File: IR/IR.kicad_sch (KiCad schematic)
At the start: 211 parts

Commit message: 回路設計
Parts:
- removed U? (x15): TSSP58038, OptoDevice:Vishay_MINICAST-3Pin, symbol Sensor_Proximity:TSSP58038
- added U10, U11, U12, U13, U14, U15, U16, U17, U2, U3, U4, U6, U7, U8, U9: TSSP58038, TSSP58038:TSSP58038_LongPad, symbol Sensor_Proximity:TSSP58038
- D12, D13, D14, D15, D16, D17, D18, D19, D20, D21, D22, D23, D24, D25, D26, D27: renamed from D?; footprint (none) -> LED_THT:LED_D3.0mm_Horizontal_O1.27mm_Z2.0mm
- U1: renamed from U?; footprint OptoDevice:Vishay_MINICAST-3Pin -> TSSP58038:TSSP58038_LongPad
- gave numbers to parts that had none: 179
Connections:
- net +3.3V: now also U10.3 (Vs), U11.3 (Vs), U12.3 (Vs), U13.3 (Vs), U14.3 (Vs), U15.3 (Vs), U16.3 (Vs), U17.3 (Vs), U2.3 (Vs), U3.3 (Vs), U4.3 (Vs), U6.3 (Vs), U7.3 (Vs), U8.3 (Vs), U9.3 (Vs)
- net GND: now also U10.2 (GND), U11.2 (GND), U12.2 (GND), U13.2 (GND), U14.2 (GND), U15.2 (GND), U16.2 (GND), U17.2 (GND), U2.2 (GND), U3.2 (GND), U4.2 (GND), U6.2 (GND), U7.2 (GND), U8.2 (GND), U9.2 (GND)
- net IR_rcpt1: now also U2.1 (OUT)
- net IR_rcpt10: now also U12.1 (OUT)
- net IR_rcpt11: now also U13.1 (OUT)
- net IR_rcpt12: now also U14.1 (OUT)
- net IR_rcpt13: now also U15.1 (OUT)
- net IR_rcpt14: now also U16.1 (OUT)
- net IR_rcpt15: now also U17.1 (OUT)
- net IR_rcpt2: now also U3.1 (OUT)
- net IR_rcpt3: now also U4.1 (OUT)
- net IR_rcpt4: now also U6.1 (OUT)
- net IR_rcpt5: now also U7.1 (OUT)
- net IR_rcpt6: now also U8.1 (OUT)
- net IR_rcpt7: now also U9.1 (OUT)
- net IR_rcpt8: now also U10.1 (OUT)
- net IR_rcpt9: now also U11.1 (OUT)

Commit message: 構成図追加
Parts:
- removed J2: Conn_01x10_Female, Connector_IDC:IDC-Header_2x05_P2.54mm_Horizontal, symbol Connector:Conn_01x10_Female
- added J2: Conn_01x10_Male, BoxHeader_1.27mm:BoxHeader_2x05_P1.27mm_Vertical_SMD, symbol Connector:Conn_01x10_Male
- added R103, R104, R105: 5.1k, Resistor_SMD:R_0402_1005Metric, symbol Device:R
- added R106, R107, R108, R109: 10k, Resistor_SMD:R_0402_1005Metric, symbol Device:R
- Q11, Q12, Q5, Q7, Q9: value 2PB709AR -> S8050; footprint Package_TO_SOT_SMD:SC-59_Handsoldering -> Package_TO_SOT_SMD:SOT-23
- SW3: footprint (none) -> Slide_Switch:SW_Slide_SPDT_White
- Y1: footprint (none) -> Crystal:Crystal_SMD_HC49-SD_HandSoldering
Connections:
- net 3.3VBUS: now also J2.1 (Pin_1)
- net Blightness_2nd: now also R107.1
- net Blightness_3rd: now also R108.1
- net Blightness_Max: now also R106.1
- net Blightness_Min: now also R109.1
- net GND: now also R32.1, R33.1, J2.4 (Pin_4), R103.1, R104.1, R105.1, R106.2, R107.2, R108.2, R109.2; no longer R32.2, R33.2
- net MainRX_STLinkTX: now also J2.8 (Pin_8)
- net MainTX_STLinkRX: now also J2.9 (Pin_9)
- net Mux_IN0: now also R103.2
- net Mux_IN1: now also R104.2
- net Mux_IN2: now also R105.2
- net Mux_OUT0: now also R32.2; no longer R32.1
- net Mux_OUT1: now also R33.2; no longer R33.1
- net NRST: now also J2.6 (Pin_6)
- net TCK: now also J2.3 (Pin_3)
- net TMS: now also J2.5 (Pin_5)
- no-connect marks 19 -> 5
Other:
- note added: "PullDown"
- moved on the sheet: Q13, Q14, Q15, U18, U19

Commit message: diagram_SmallPW
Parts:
- removed C1, C14: 4.7uF, Capacitor_SMD:C_0603_1608Metric, symbol Device:C
- added C? (x2): 1uF, Capacitor_SMD:C_0402_1005Metric, symbol Device:C
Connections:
- net 3.3VSYS: now also C?.1
- net S-S: now also C?.1
- net at Q3.1 (G), R4.2, R8.1: now also C?.2
- net at Q8.1 (G), R22.2, R24.1: now also C?.2
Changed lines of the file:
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@@
     (pin "3")
   )
+  (symbol (lib_id "Device:C") (at 124.46 142.24 0) (unit 1)
+    (in_bom yes) (on_board yes) (fields_autoplaced)
+    (property "Reference" "C?" (id 0) (at 128.27 140.9699 0)
+      (effects (font (size 1.27 1.27)) (justify left))
+    )
+    (property "Value" "1uF" (id 1) (at 128.27 143.5099 0)
+      (effects (font (size 1.27 1.27)) (justify left))
+    )
+    (property "Footprint" "Capacitor_SMD:C_0402_1005Metric" (id 2) (at 125.4252 146.05 0)
+      (effects (font (size 1.27 1.27)) hide)
+    )
+    (property "Datasheet" "~" (id 3) (at 124.46 142.24 0)
+      (effects (font (size 1.27 1.27)) hide)
+    )
+    (pin "1")
+    (pin "2")
+  )
   (symbol (lib_id "power:GND") (at 355.6 109.22 0) (mirror y) (unit 1)
     (in_bom yes) (on_board yes)
@@
     (pin "2")
   )
-  (symbol (lib_id "Device:C") (at 248.92 86.36 0) (unit 1)
-    (in_bom yes) (on_board yes) (fields_autoplaced)
-    (property "Reference" "C14" (id 0) (at 252.73 85.0899 0)
-      (effects (font (size 1.27 1.27)) (justify left))
-    )
-    (property "Value" "4.7uF" (id 1) (at 252.73 87.6299 0)
-      (effects (font (size 1.27 1.27)) (justify left))
-    )
-    (property "Footprint" "Capacitor_SMD:C_0603_1608Metric" (id 2) (at 249.8852 90.17 0)
-      (effects (font (size 1.27 1.27)) hide)
-    )
-    (property "Datasheet" "~" (id 3) (at 248.92 86.36 0)
-      (effects (font (size 1.27 1.27)) hide)
-    )
-    (pin "1")
-    (pin "2")
-  )
   (symbol (lib_id "power:VDD") (at 721.36 248.92 0) (unit 1)
     (in_bom yes) (on_board yes) (fields_autoplaced)
@@
     (pin "2")
   )
+  (symbol (lib_id "Device:C") (at 248.92 86.36 0) (unit 1)
+    (in_bom yes) (on_board yes) (fields_autoplaced)
+    (property "Reference" "C?" (id 0) (at 252.73 85.0899 0)
+      (effects (font (size 1.27 1.27)) (justify left))
+    )
+    (property "Value" "1uF" (id 1) (at 252.73 87.6299 0)
+      (effects (font (size 1.27 1.27)) (justify left))
+    )
+    (property "Footprint" "Capacitor_SMD:C_0402_1005Metric" (id 2) (at 249.8852 90.17 0)
+      (effects (font (size 1.27 1.27)) hide)
+    )
+    (property "Datasheet" "~" (id 3) (at 248.92 86.36 0)
+      (effects (font (size 1.27 1.27)) hide)
+    )
+    (pin "1")
+    (pin "2")
+  )
   (symbol (lib_id "Device:R") (at 193.04 365.76 270) (mirror x) (unit 1)
     (in_bom yes) (on_board yes)
@@
     (pin "2")
   )
-  (symbol (lib_id "Device:C") (at 124.46 142.24 0) (unit 1)
-    (in_bom yes) (on_board yes) (fields_autoplaced)
-    (property "Reference" "C1" (id 0) (at 128.27 140.9699 0)
-      (effects (font (size 1.27 1.27)) (justify left))
-    )
-    (property "Value" "4.7uF" (id 1) (at 128.27 143.5099 0)
-      (effects (font (size 1.27 1.27)) (justify left))
-    )
-    (property "Footprint" "Capacitor_SMD:C_0603_1608Metric" (id 2) (at 125.4252 146.05 0)
-      (effects (font (size 1.27 1.27)) hide)
-    )
-    (property "Datasheet" "~" (id 3) (at 124.46 142.24 0)
-      (effects (font (size 1.27 1.27)) hide)
-    )
-    (pin "1")
-    (pin "2")
-  )
   (symbol (lib_id "Device:R") (at 607.06 386.08 0) (unit 1)
     (in_bom yes) (on_board yes)
@@
       (reference "#PWR0218") (unit 1) (value "+3.3V") (footprint "")
     )
-    (path "/d3fd32d8-94e9-4c99-93a7-2be4594e1c1d"
-      (reference "C1") (unit 1) (value "4.7uF") (footprint "Capacitor_SMD:C_0603_1608Metric")
-    )
     (path "/3be126c6-ab05-4a33-b739-124117490790"
       (reference "C2") (unit 1) (value "0.1uF") (footprint "Capacitor_SMD:C_0402_1005Metric")
@@
       (reference "C13") (unit 1) (value "ADJ_ST") (footprint "Capacitor_SMD:C_0603_1608Metric")
     )
-    (path "/7ac18cd6-3e4d-45f8-a364-a40e9c7e4e34"
-      (reference "C14") (unit 1) (value "4.7uF") (footprint "Capacitor_SMD:C_0603_1608Metric")
-    )
     (path "/d5678bbb-1b01-4cf0-b614-a52145100a78"
       (reference "C15") (unit 1) (value "0.1uF") (footprint "Capacitor_SMD:C_0402_1005Metric")
@@
       (reference "C29") (unit 1) (value "0.1uF") (footprint "Capacitor_SMD:C_0402_1005Metric")
     )
+    (path "/1ece6ebb-c400-4888-b100-b48233656f5d"
+      (reference "C?") (unit 1) (value "1uF") (footprint "Capacitor_SMD:C_0402_1005Metric")
+    )
+    (path "/82205771-b21f-43e1-8b52-616b847379d7"
+      (reference "C?") (unit 1) (value "1uF") (footprint "Capacitor_SMD:C_0402_1005Metric")
+    )
     (path "/c1ae4c9b-7bc6-48f5-82c2-85b204b6b5a6"

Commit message: 進捗
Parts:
- D1, D2: value SBR1A40SA -> 1N5819WS; footprint Diode_SMD:D_SMA_Handsoldering -> Diode_SMD:D_SOD-323_HandSoldering
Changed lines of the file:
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@@
       (effects (font (size 1.27 1.27)) (justify left))
     )
-    (property "Value" "SBR1A40SA" (id 1) (at 149.86 162.56 90)
-      (effects (font (size 1.27 1.27)) (justify left))
-    )
-    (property "Footprint" "Diode_SMD:D_SMA_Handsoldering" (id 2) (at 147.32 154.94 0)
+    (property "Value" "1N5819WS" (id 1) (at 149.86 162.56 90)
+      (effects (font (size 1.27 1.27)) (justify left))
+    )
+    (property "Footprint" "Diode_SMD:D_SOD-323_HandSoldering" (id 2) (at 147.32 154.94 0)
       (effects (font (size 1.27 1.27)) hide)
     )
@@
     (in_bom yes) (on_board yes) (fields_autoplaced)
     (property "Reference" "D2" (id 0) (at 195.2625 74.93 0))
-    (property "Value" "SBR1A40SA" (id 1) (at 195.2625 77.47 0))
-    (property "Footprint" "Diode_SMD:D_SMA_Handsoldering" (id 2) (at 195.58 81.28 0)
+    (property "Value" "1N5819WS" (id 1) (at 195.2625 77.47 0))
+    (property "Footprint" "Diode_SMD:D_SOD-323_HandSoldering" (id 2) (at 195.58 81.28 0)
       (effects (font (size 1.27 1.27)) hide)
     )
@@
     )
     (path "/c1ae4c9b-7bc6-48f5-82c2-85b204b6b5a6"
-      (reference "D1") (unit 1) (value "SBR1A40SA") (footprint "Diode_SMD:D_SMA_Handsoldering")
+      (reference "D1") (unit 1) (value "1N5819WS") (footprint "Diode_SMD:D_SOD-323_HandSoldering")
     )
     (path "/da552608-6f61-41ba-8dd6-88bb12b74d81"
-      (reference "D2") (unit 1) (value "SBR1A40SA") (footprint "Diode_SMD:D_SMA_Handsoldering")
+      (reference "D2") (unit 1) (value "1N5819WS") (footprint "Diode_SMD:D_SOD-323_HandSoldering")
     )
     (path "/83b8239d-b6f8-407a-8031-4de274681425"

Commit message: エンコーダー基板配線完了
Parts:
- removed C24: 22pF, Capacitor_SMD:C_0603_1608Metric, symbol Device:C
- removed Y1: 48MHz, Crystal:Crystal_SMD_HC49-SD_HandSoldering, symbol Device:Crystal
- added C30, C31: 0.1uF, Capacitor_SMD:C_0402_1005Metric, symbol Device:C
- added U22: NJU6319AE, Package_SO:SOP-8_3.9x4.9mm_P1.27mm, symbol CrystalOSC_Control:NJU6319AE
- added Y1: 16MHz, Crystal:Crystal_SMD_3225-4Pin_3.2x2.5mm_HandSoldering, symbol Device:Crystal_GND24
- C23: value 22pF -> 0.1uF; footprint Capacitor_SMD:C_0603_1608Metric -> Capacitor_SMD:C_0402_1005Metric
- gave numbers to parts that had none: 2
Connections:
- net +3.3V: now also C23.1, C30.1, C31.1, U22.1 (~{CONT}), U22.8 (VDD)
- net GND: now also C23.2, C30.2, C31.2, U22.4 (VSS), Y1.2, Y1.4; no longer C23.1
- net NRST: now also U20.6 (PF2-NRST)
- net OSC_IN: now also U20.2 (PC14-OSCX_IN), U22.5 (FOUT); no longer C23.2
- new net: U22.2 (XT), Y1.1
- new net: U22.3 (~{XT}), Y1.3
- new net: U22.6 (NC), U22.7 (NC)
- no-connect marks 5 -> 6
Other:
- moved on the sheet: C26

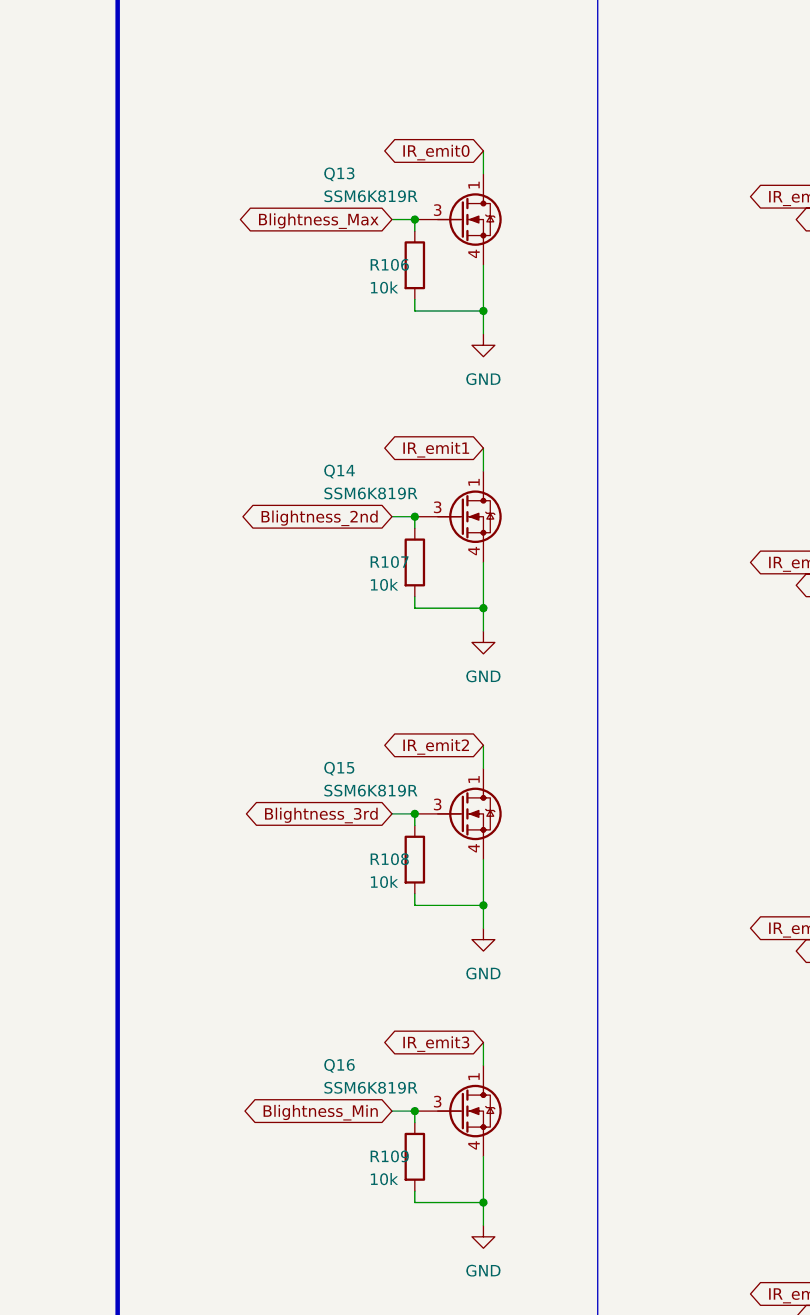
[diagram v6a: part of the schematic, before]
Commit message: 人力曲面配線中
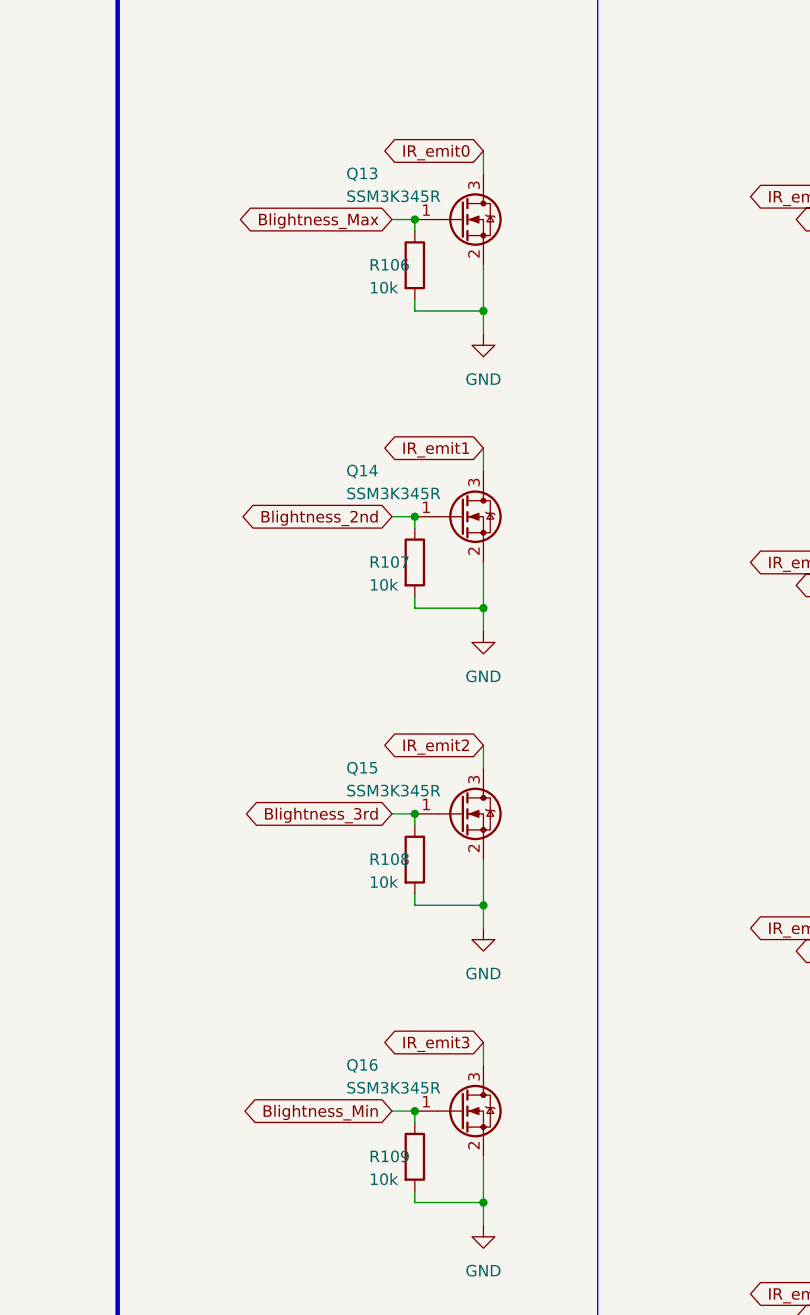
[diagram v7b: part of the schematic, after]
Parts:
- removed Q13, Q14, Q15, Q16: SSM6K819R, TSOP6F:SSM6J808R, symbol Transistor_FET:Si1442DH
- added Q13, Q14, Q15, Q16: SSM3K345R, Package_TO_SOT_SMD:SOT-23W, symbol Device:Q_NMOS_GSD
- D12, D13, D14, D15, D16, D17, D18, D19, D20, D21, D22, D23, D24, D25, D26, D27: footprint LED_THT:LED_D3.0mm_Horizontal_O1.27mm_Z2.0mm -> LED_3.0mm_Center:LED_D3.0mm_Horizontal_O1.27mm_Z2.0mm
- J1: footprint Connector_Molex:Molex_SPOX_5268-02A_1x02_P2.50mm_Horizontal -> Connector_Molex:Molex_SPOX_5267-02A_1x02_P2.50mm_Vertical
- J3, J4: footprint Connector_Molex:Molex_SPOX_5268-04A_1x04_P2.50mm_Horizontal -> Connector_Molex:Molex_SPOX_5267-04A_1x04_P2.50mm_Vertical
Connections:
- net Blightness_2nd: now also Q14.1 (G)
- net Blightness_3rd: now also Q15.1 (G)
- net Blightness_Max: now also Q13.1 (G)
- net Blightness_Min: now also Q16.1 (G)
- net GND: now also Q13.2 (S), Q14.2 (S), Q15.2 (S), Q16.2 (S)
- net IR_emit0: now also Q13.3 (D)
- net IR_emit1: now also Q14.3 (D)
- net IR_emit2: now also Q15.3 (D)
- net IR_emit3: now also Q16.3 (D)

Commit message: IR半分
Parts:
- removed C13: ADJ_ST, Capacitor_SMD:C_0603_1608Metric, symbol Device:C
- removed C14: 1uF, Capacitor_SMD:C_0402_1005Metric, symbol Device:C
- removed C2: 0.1uF, Capacitor_SMD:C_0402_1005Metric, symbol Device:C
- removed D10, D9: Green, LED_SMD:LED_0603_1608Metric_Pad1.05x0.95mm_HandSolder, symbol Device:LED
- removed D7: D_Zener, Diode_SMD:D_SOD-323_HandSoldering, symbol Device:D_Zener
- removed H1, H2: MountingHole_Pad, TestPoint:TestPoint_Pad_1.5x1.5mm, symbol Mechanical:MountingHole_Pad
- removed Q10, Q4, Q6, Q8: SSM3J332R, Package_TO_SOT_SMD:SOT-23W, symbol Device:Q_PMOS_GSD
- removed Q11, Q5, Q7, Q9: S8050, Package_TO_SOT_SMD:SOT-23, symbol Device:Q_PNP_BEC
- removed R16, R18, R20, R21, R23, R24, R25, R26, R27: 10k, Resistor_SMD:R_0402_1005Metric, symbol Device:R
- removed R19, R29, R30: 1k, Resistor_SMD:R_0402_1005Metric, symbol Device:R
- removed R22: 100k, Resistor_SMD:R_0402_1005Metric, symbol Device:R
- U20: value STM32C031K4T6 -> STM32G030K6T6
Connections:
- net 3.3VSYS is gone; now on net +3.3V: C8.1, D2.2 (A), R17.2, U5.2 (VO)
- net Blightness_2nd: now also U20.14 (PA7)
- net Blightness_3rd: now also U20.15 (PB0)
- net Blightness_Max: now also U20.13 (PA6)
- net Blightness_Min: now also U20.16 (PB1)
- net DIP_SW0: now also U20.29 (PB5)
- net DIP_SW1: now also U20.28 (PB4)
- net DIP_SW2: now also U20.27 (PB3)
- net DIP_SW3: now also U20.23 (PA12[PA10])
- net DIP_SW4: now also U20.22 (PA11[PA9])
- net LED0: now also U20.30 (PB6)
- net LED1: now also U20.1 (PB9)
- net LED2: now also U20.32 (PB8)
- net MainRX_RS485TX: now also U20.26 (PA15)
- net MainRX_STLinkTX: now also U20.21 (PA10)
- net MainTX_RS485RX: now also U20.9 (PA2)
- net MainTX_STLinkRX: now also U20.19 (PA9)
- net MonitorLED0: now also U20.31 (PB7)
- net Mux_IN0: now also U20.12 (PA5)
- net Mux_IN1: now also U20.11 (PA4)
- net Mux_IN2: now also U20.10 (PA3)
- net Mux_OUT0: now also U20.8 (PA1)
- net Mux_OUT1: now also U20.7 (PA0)
- net Slide_SW0: now also U20.20 (PC6)
- net TCK: now also U20.25 (PA14-BOOT0)
- net TMS: now also U20.24 (PA13)
- net 3.3VBUS: no longer names the net of J2.1 (Pin_1)
- no-connect marks 6 -> 8
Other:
- note removed: "理想ダイオード/3.3VSYS"
- note removed: "電源切替/STLink"
- moved on the sheet: C27, C28, C7, C8, D11, D2, D8, R17, R28, R31, TP1, TP2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
